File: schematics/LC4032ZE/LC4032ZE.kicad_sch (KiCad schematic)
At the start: 280 parts

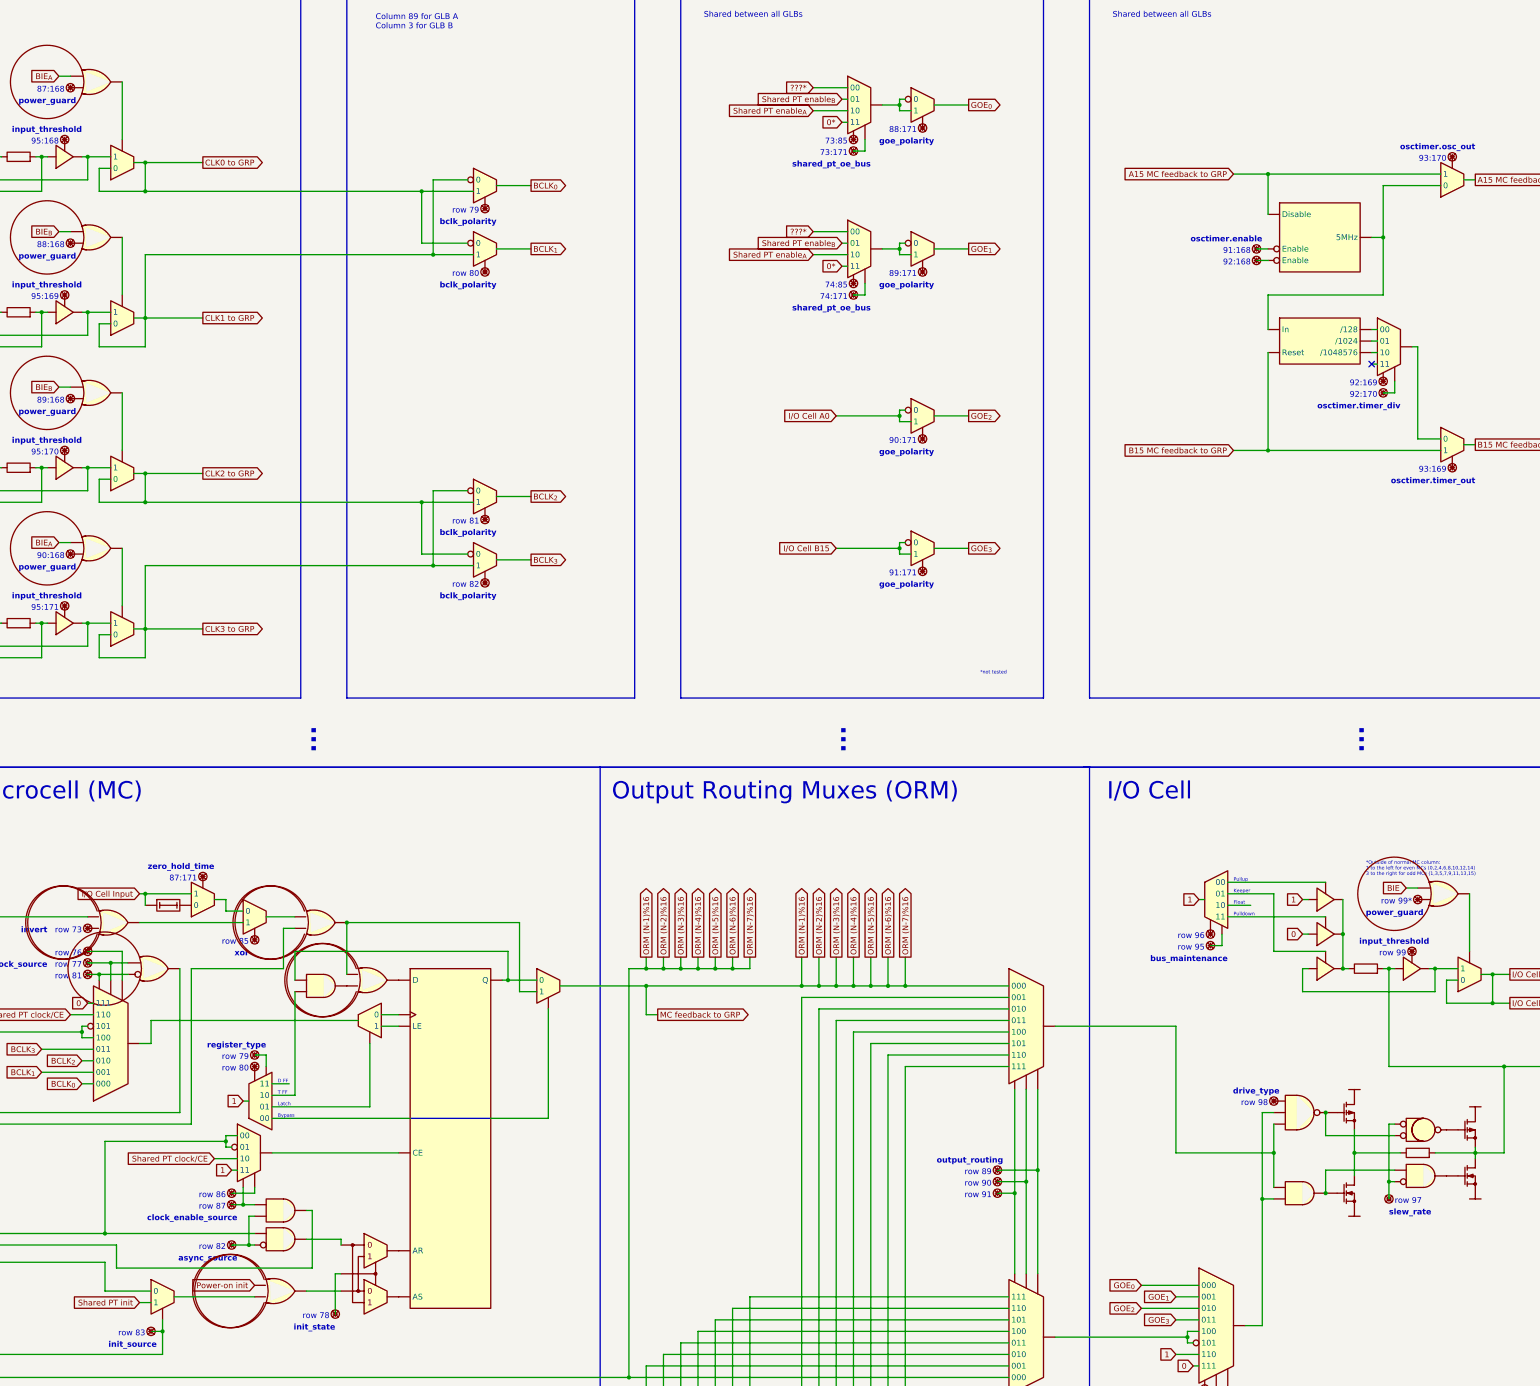
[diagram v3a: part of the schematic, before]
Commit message: refactor reg_type => mc_func to match common.MacrocellFunction
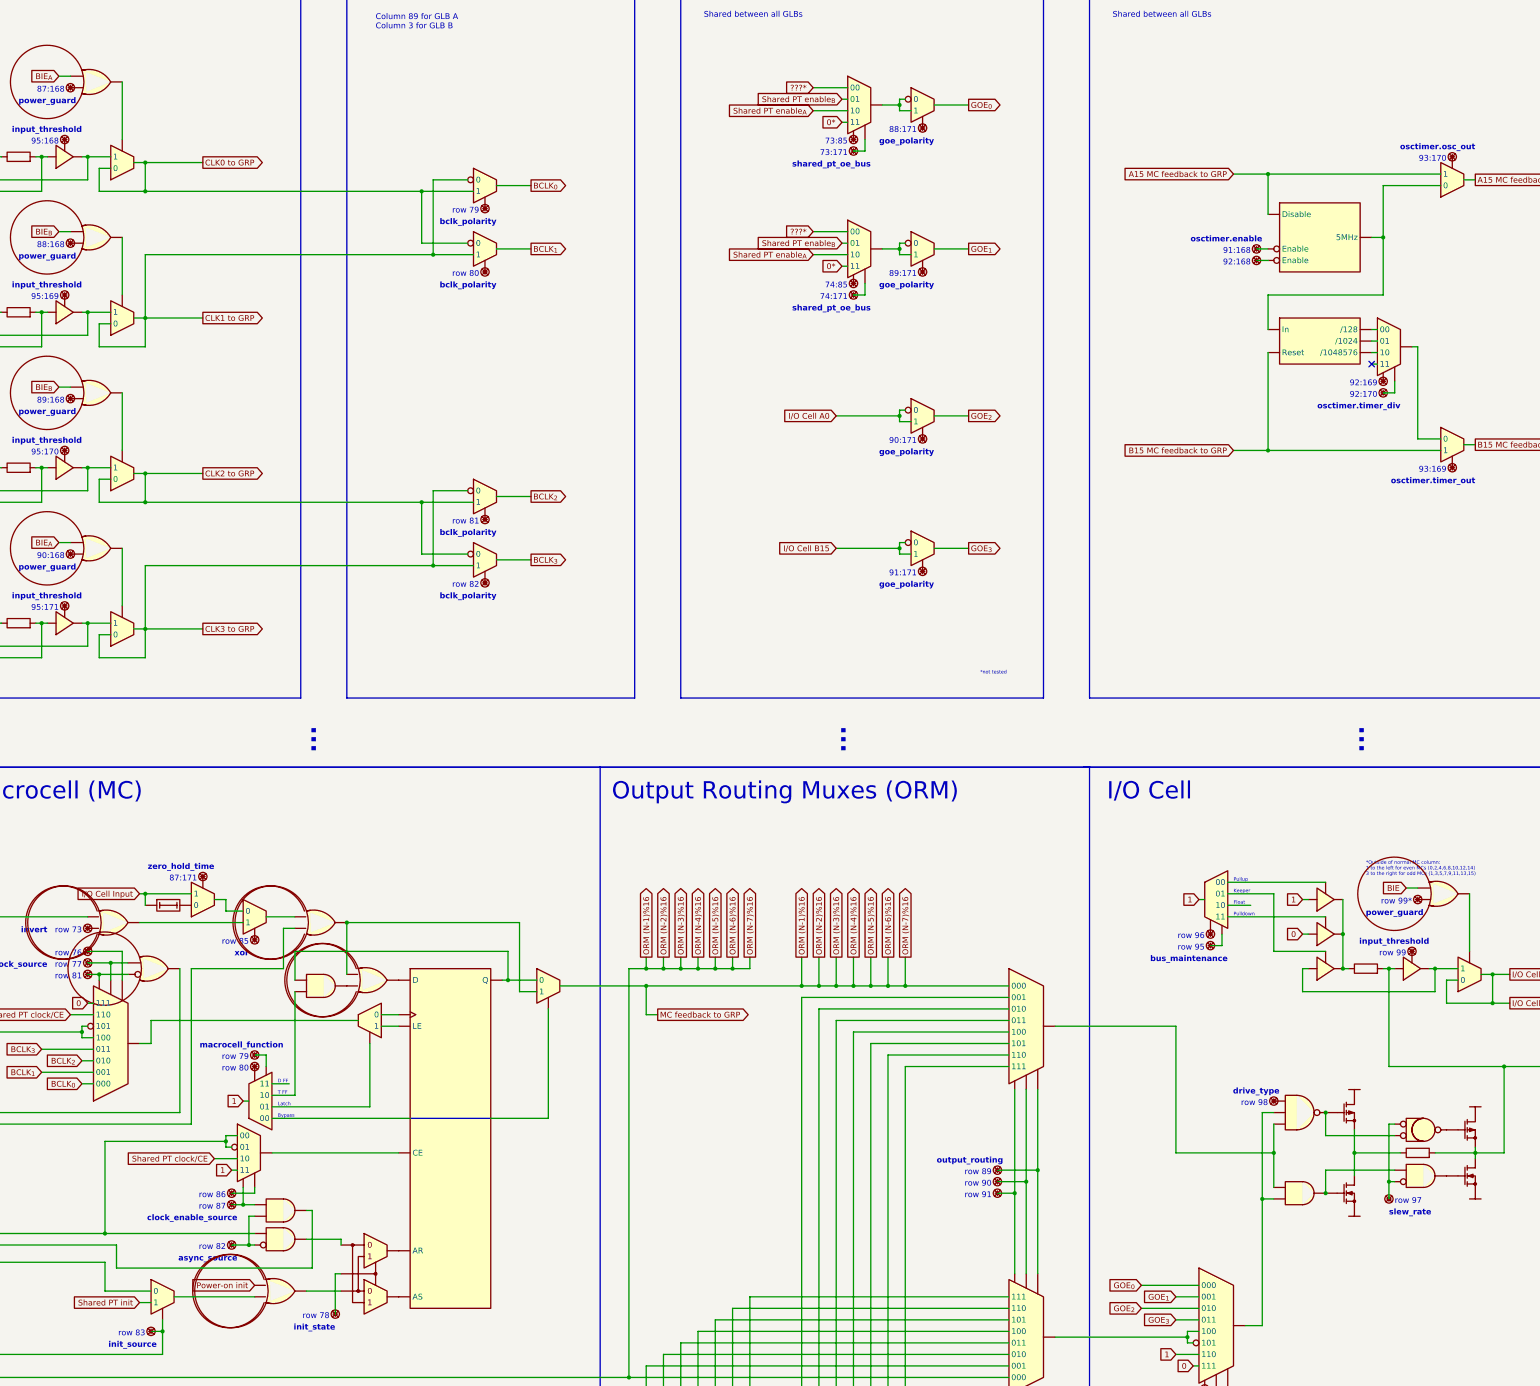
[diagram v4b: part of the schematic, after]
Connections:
- net at U?.: now also R?.1, U?., U?.; no longer U?.
- net at U?.: now also F?.; no longer U?. (Q)
- net at U?. (Q): now also U?.; no longer U?.
- net at U?.: now also U?., U?., U?.; no longer U?.
- net at U?.: now also U?.; no longer U?. (Q) (x2)
- net at U?.: now also U?.; no longer U?. (x7)
- net at U?.: now also U?., U?.; no longer U?. (x2)
- net at U?., U?.: now also U?. (x3)
- net at U?.: no longer U?.
- net at U?.: now also F?., U?.; no longer U?.
- net at U?.: now also F?.; no longer U?.
- net at U?., U?.: now also U?.; no longer U?.
- new net: R?.1, U?., U?., U?. (x4)
- new net: U?., U?. (x43)
- new net: U?., U?. (Q) (x5)
- new net: U?., U?., U?. (x8)
- new net: Q?., Q?., R?.1
- new net: Q?., U?., U?. (x2)
- new net: U?., U?., U?. (Q)
- new net: F?., U?., U?. (x8)
- new net: U?., U?. (Enable), U?. (Reset)
- new net: U?., U?. (Reset) (x3)
- now unconnected: U?., U?., U?.
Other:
- note added: "macrocell_function"
- note removed: "register_type"
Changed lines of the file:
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@@
     (effects (font (size 1.27 1.27) (thickness 0.254) bold) (justify right bottom))
   )
-  (text "register_type" (at 350.52 255.27 180)
+  (text "macrocell_function" (at 354.33 255.27 180)
     (effects (font (size 1.27 1.27) (thickness 0.254) bold) (justify right bottom))
   )

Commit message: Adjustments for LC4k More fixes for LC4064ZC_csBGA56
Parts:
- U?: symbol symbols:AND2 -> symbols:AND2_N1
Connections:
- net at U?.: now also R?.1, U?., U?.; no longer U?.
- net at U?.: now also F?.; no longer U?. (Q)
- net at U?. (Q): now also U?.; no longer U?.
- net at U?.: now also U?., U?., U?.; no longer U?.
- net at U?.: now also U?.; no longer U?. (Q) (x2)
- net at U?.: now also U?.; no longer U?. (x7)
- net at U?.: now also U?., U?.; no longer U?. (x2)
- net at U?., U?.: now also U?. (x3)
- net at U?.: no longer U?.
- net at U?.: now also F?., U?.; no longer U?.
- net at U?.: now also F?.; no longer U?.
- net at U?., U?.: now also U?.; no longer U?.
- new net: R?.1, U?., U?., U?. (x4)
- new net: U?., U?. (x43)
- new net: U?., U?. (Q) (x5)
- new net: U?., U?., U?. (x8)
- new net: Q?., Q?., R?.1
- new net: Q?., U?., U?. (x2)
- new net: U?., U?., U?. (Q)
- new net: F?., U?., U?. (x8)
- new net: U?., U?. (Enable), U?. (Reset)
- new net: U?., U?. (Reset) (x3)
- now unconnected: U?., U?., U?.
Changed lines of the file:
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@@
   (junction (at 110.49 394.97) (diameter 0) (color 0 0 0 0)
   )
-  (junction (at 115.57 420.37) (diameter 0) (color 0 0 0 0)
-  )
   (junction (at 153.67 369.57) (diameter 0) (color 0 0 0 0)
   )
@@
   (junction (at 453.39 237.49) (diameter 0) (color 0 0 0 0)
   )
-  (junction (at 138.43 420.37) (diameter 0) (color 0 0 0 0)
-  )
   (junction (at 115.57 213.36) (diameter 0) (color 0 0 0 0)
   )
@@
   (junction (at 110.49 264.16) (diameter 0) (color 0 0 0 0)
   )
-  (junction (at 110.49 420.37) (diameter 0) (color 0 0 0 0)
-  )
   (junction (at 617.22 278.13) (diameter 0) (color 0 0 0 0)
   )
@@
   (junction (at 596.9 76.2) (diameter 0) (color 0 0 0 0)
   )
-  (junction (at 148.59 420.37) (diameter 0) (color 0 0 0 0)
-  )
   (junction (at 290.83 92.71) (diameter 0) (color 0 0 0 0)
   )
@@
   (junction (at 311.15 161.29) (diameter 0) (color 0 0 0 0)
   )
-  (junction (at 125.73 420.37) (diameter 0) (color 0 0 0 0)
-  )
   (junction (at 125.73 394.97) (diameter 0) (color 0 0 0 0)
   )
@@
   (junction (at 143.51 289.56) (diameter 0) (color 0 0 0 0)
   )
-  (junction (at 120.65 420.37) (diameter 0) (color 0 0 0 0)
-  )
   (junction (at 588.01 237.49) (diameter 0) (color 0 0 0 0)
   )
@@
   (junction (at 387.35 80.01) (diameter 0) (color 0 0 0 0)
   )
-  (junction (at 143.51 420.37) (diameter 0) (color 0 0 0 0)
-  )
   (junction (at 384.81 134.62) (diameter 0) (color 0 0 0 0)
   )
   (junction (at 341.63 275.59) (diameter 0) (color 0 0 0 0)
   )
-  (junction (at 153.67 420.37) (diameter 0) (color 0 0 0 0)
-  )
   (junction (at 468.63 241.3) (diameter 0) (color 0 0 0 0)
   )
@@
     (stroke (width 0) (type default) (color 0 0 0 0))
   )
-  (wire (pts (xy 143.51 420.37) (xy 143.51 445.77))
-    (stroke (width 0) (type default) (color 0 0 0 0))
-  )
   (wire (pts (xy 299.72 92.71) (xy 300.99 92.71))
     (stroke (width 0) (type default) (color 0 0 0 0))
@@
     (stroke (width 0) (type default) (color 0 0 0 0))
   )
-  (wire (pts (xy 110.49 420.37) (xy 110.49 445.77))
-    (stroke (width 0) (type default) (color 0 0 0 0))
-  )
   (wire (pts (xy 457.2 234.95) (xy 457.2 237.49))
     (stroke (width 0) (type default) (color 0 0 0 0))
@@
     (stroke (width 0) (type default) (color 0 0 0 0))
   )
-  (wire (pts (xy 148.59 420.37) (xy 148.59 445.77))
-    (stroke (width 0) (type default) (color 0 0 0 0))
-  )
   (wire (pts (xy 480.06 251.46) (xy 480.06 331.47))
     (stroke (width 0) (type default) (color 0 0 0 0))
@@
     (stroke (width 0) (type default) (color 0 0 0 0))
   )
-  (wire (pts (xy 153.67 420.37) (xy 153.67 445.77))
-    (stroke (width 0) (type default) (color 0 0 0 0))
-  )
   (wire (pts (xy 120.65 167.64) (xy 120.65 213.36))
     (stroke (width 0) (type default) (color 0 0 0 0))
@@
     (stroke (width 0) (type default) (color 0 0 0 0))
   )
-  (wire (pts (xy 125.73 420.37) (xy 125.73 445.77))
-    (stroke (width 0) (type default) (color 0 0 0 0))
-  )
   (wire (pts (xy 143.51 314.96) (xy 143.51 369.57))
     (stroke (width 0) (type default) (color 0 0 0 0))
@@
     (stroke (width 0) (type default) (color 0 0 0 0))
   )
-  (wire (pts (xy 115.57 420.37) (xy 115.57 445.77))
-    (stroke (width 0) (type default) (color 0 0 0 0))
-  )
   (wire (pts (xy 153.67 167.64) (xy 153.67 213.36))
     (stroke (width 0) (type default) (color 0 0 0 0))
@@
     (stroke (width 0) (type default) (color 0 0 0 0))
   )
-  (wire (pts (xy 120.65 420.37) (xy 120.65 445.77))
-    (stroke (width 0) (type default) (color 0 0 0 0))
-  )
   (wire (pts (xy 566.42 316.23) (xy 570.23 316.23))
     (stroke (width 0) (type default) (color 0 0 0 0))
@@
     (stroke (width 0) (type default) (color 0 0 0 0))
   )
-  (wire (pts (xy 138.43 420.37) (xy 138.43 445.77))
-    (stroke (width 0) (type default) (color 0 0 0 0))
-  )
   (wire (pts (xy 151.765 403.225) (xy 151.765 403.86))
     (stroke (width 0) (type default) (color 0 0 0 0))
@@
     (pin "")
   )
-  (symbol (lib_id "symbols:AND2") (at 575.31 287.02 0) (unit 1)
+  (symbol (lib_id "symbols:AND2_N1") (at 575.31 287.02 0) (mirror x) (unit 1)
     (in_bom yes) (on_board yes) (fields_autoplaced)
-    (property "Reference" "U?" (id 0) (at 571.5 292.1 0)
+    (property "Reference" "U?" (id 0) (at 571.5 281.94 0)
       (effects (font (size 1.27 1.27)) hide)
     )
-    (property "Value" "AND2" (id 1) (at 581.66 281.94 0)
+    (property "Value" "AND2" (id 1) (at 581.66 292.1 0)
       (effects (font (size 1.27 1.27)) hide)
     )

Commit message: Add notes on multiple GLBs driving same PT OE bus line
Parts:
- removed F? (x3): Fuse, symbol symbols:Fuse
- removed U?: Microinverter, symbol symbols:Microinverter
- removed U?: Mux2, symbol symbols:Mux2
- removed U? (x2): Mux4, symbol symbols:Mux4
- added F? (x3): Fuse, symbol symbols:Fuse
- added U? (x5): Mux2, symbol symbols:Mux2
- added U?: Microinverter, symbol symbols:Microinverter
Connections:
- net 1: now also U?., U?.
- net GI_{0}: no longer U?., U?., U?., U?., U?., U?., U?., U?., U?.
- net GI_{1}: no longer U?., U?., U?., U?., U?., U?., U?., U?., U?.
- net GI_{34}: now also U?., U?., U?., U?., U?., U?., U?., U?.
- net GI_{35}: now also U?., U?., U?., U?., U?., U?., U?., U?.
- net GOE_{0}: now also U?.
- net Shared PT enable_{A}: now also U?., U?.
- net Shared PT enable_{B}: now also U?., U?.
- net ~{GI_{0}}: no longer U?., U?., U?., U?., U?., U?., U?., U?., U?.
- net ~{GI_{1}}: no longer U?., U?., U?., U?., U?., U?., U?., U?., U?.
- net at U?.: now also R?.1, U?., U?.; no longer U?.
- net at U?.: now also F?.; no longer U?. (Q)
- net at U?. (Q): now also U?.; no longer U?.
- net at U?.: now also U?., U?., U?.; no longer U?.
- net at U?.: now also U?.; no longer U?. (Q) (x2)
- net at U?.: now also U?.; no longer U?. (x7)
- net ~{GI_{34}}: now reaches U?.
- net ~{GI_{34}}: now also U?., U?., U?., U?., U?., U?., U?., U?.
- net at U?.: now also U?., U?.; no longer U?. (x2)
- net at U?., U?.: now also U?. (x2)
- net at U?.: no longer U?.
- net ~{GI_{35}}: now reaches U?.
- net ~{GI_{35}}: now also U?., U?., U?., U?., U?., U?., U?., U?.
- net at U?.: now also F?., U?.; no longer U?.
- net at U?.: now also F?.; no longer U?.
- net at U?., U?.: now also U?.; no longer U?.
- net at F?.: now also U?. (x2)
- new net: R?.1, U?., U?., U?. (x4)
- new net: U?., U?. (x45)
- new net: U?., U?. (Q) (x5)
- new net: U?., U?., U?. (x9)
- new net: Q?., Q?., R?.1
- new net: Q?., U?., U?. (x2)
- new net: U?., U?., U?. (Q)
- new net: F?., U?., U?. (x8)
- new net: F?., U?. (x3)
- new net: U?., U?. (Enable), U?. (Reset)
- new net: U?., U?. (Reset) (x3)
- now unconnected: U?., U?., U?.
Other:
- note added: "row 75 column 171 for GLB A column 85 for GLB B"
- note removed: "*not tested"
- note removed: "row 75* column 171 for GLB A column 85 for GLB B"
